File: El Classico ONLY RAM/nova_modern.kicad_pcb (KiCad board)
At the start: 2 copper layers, 379 x 139.7 mm, 49 parts, among them J1 PORTA, J2 PORTB, SW1 SW_SPDT, U1 74LS14, U10 62256P, U11 62256P, U12 27C256, U13 7496, U14 7496, U15 7496, U16 7496, U17 74ALS00, U18 74LS241, U19 74LS241, U2 74LS14, U3 74LS14, U4 74LS14, U5 74LS14, U6 74LS148, U7 74LS148, U8 74LS148, U9 27C256

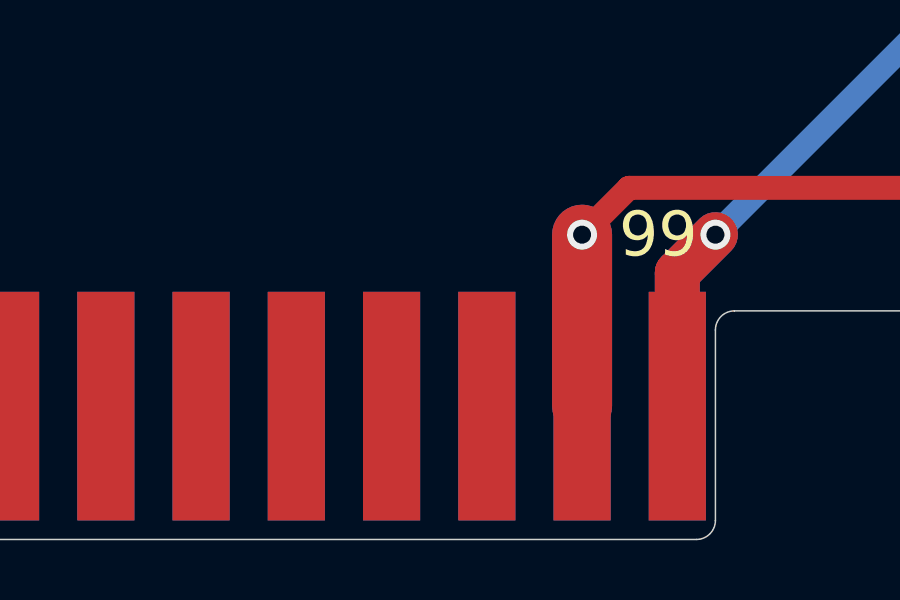
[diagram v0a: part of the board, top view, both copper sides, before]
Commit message: bridge dchp/intp in/out
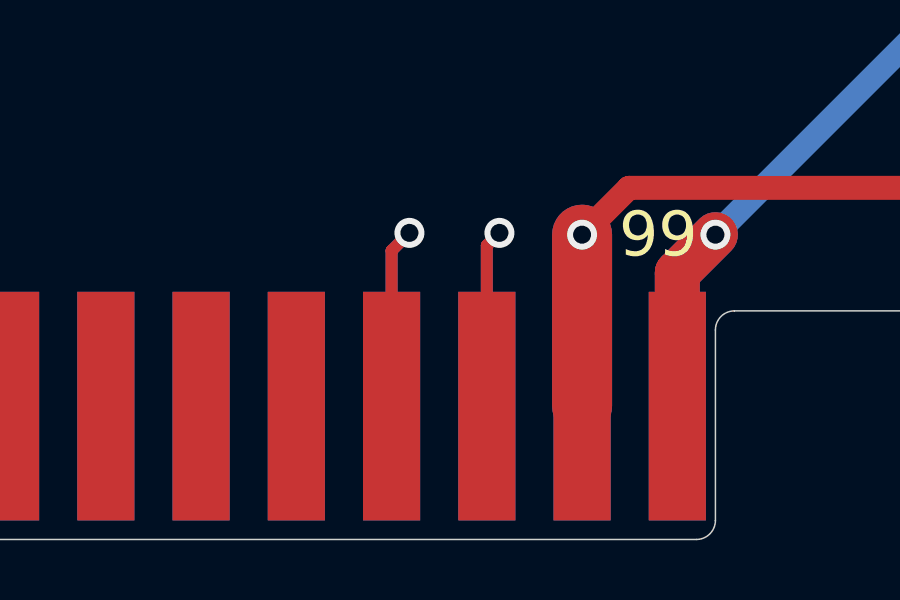
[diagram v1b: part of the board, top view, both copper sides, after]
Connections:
- J1 pad 93: unconnected-(J1-Pin_93-Pad93) -> /dchp
- J1 pad 94: unconnected-(J1-Pin_94-Pad94) -> /dchp
- J1 pad 95: unconnected-(J1-Pin_95-Pad95) -> /intp
- J1 pad 96: unconnected-(J1-Pin_96-Pad96) -> /intp
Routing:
- net /dchp: track 0.00 -> 12.0 mm, vias 0 -> 1
- net /intp: track 0.00 -> 11.9 mm, vias 0 -> 1
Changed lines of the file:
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@@
 			(size 1.905 7.62)
 			(layers "F.Cu" "F.Mask" "F.Paste")
-			(net "unconnected-(J1-Pin_93-Pad93)")
+			(net "/dchp")
 			(pinfunction "Pin_93_93")
-			(pintype "passive+no_connect")
+			(pintype "passive")
 		)
 		(pad "94" smd rect
@@
 			(size 1.905 7.62)
 			(layers "B.Cu" "B.Mask" "B.Paste")
-			(net "unconnected-(J1-Pin_94-Pad94)")
+			(net "/dchp")
 			(pinfunction "Pin_94_94")
-			(pintype "passive+no_connect")
+			(pintype "passive")
 		)
 		(pad "95" smd rect
@@
 			(size 1.905 7.62)
 			(layers "F.Cu" "F.Mask" "F.Paste")
-			(net "unconnected-(J1-Pin_95-Pad95)")
+			(net "/intp")
 			(pinfunction "Pin_95_95")
-			(pintype "passive+no_connect")
+			(pintype "passive")
 		)
 		(pad "96" smd rect
@@
 			(size 1.905 7.62)
 			(layers "B.Cu" "B.Mask" "B.Paste")
-			(net "unconnected-(J1-Pin_96-Pad96)")
+			(net "/intp")
 			(pinfunction "Pin_96_96")
-			(pintype "passive+no_connect")
+			(pintype "passive")
 		)
 		(pad "97" smd rect
@@
 		(net "/WD12")
 	)
+	(segment
+		(start 193 99)
+		(end 192.405 99.595)
+		(width 0.4)
+		(layer "F.Cu")
+		(net "/dchp")
+	)
+	(segment
+		(start 192.405 99.595)
+		(end 192.405 104.775)
+		(width 0.4)
+		(layer "F.Cu")
+		(net "/dchp")
+	)
+	(via
+		(at 193 99)
+		(size 1)
+		(drill 0.6)
+		(layers "F.Cu" "B.Cu")
+		(net "/dchp")
+	)
+	(segment
+		(start 192.405 104.775)
+		(end 192.405 99.595)
+		(width 0.4)
+		(layer "B.Cu")
+		(net "/dchp")
+	)
+	(segment
+		(start 192.405 99.595)
+		(end 193 99)
+		(width 0.4)
+		(layer "B.Cu")
+		(net "/dchp")
+	)
+	(segment
+		(start 195.58 99.42)
+		(end 195.58 104.775)
+		(width 0.4)
+		(layer "F.Cu")
+		(net "/intp")
+	)
+	(segment
+		(start 196 99)
+		(end 195.58 99.42)
+		(width 0.4)
+		(layer "F.Cu")
+		(net "/intp")
+	)
+	(via
+		(at 196 99)
+		(size 1)
+		(drill 0.6)
+		(layers "F.Cu" "B.Cu")
+		(net "/intp")
+	)
+	(segment
+		(start 195.58 99.42)
+		(end 195.58 104.775)
+		(width 0.4)
+		(layer "B.Cu")
+		(net "/intp")
+	)
+	(segment
+		(start 195.58 99.42)
+		(end 196 99)
+		(width 0.4)
+		(layer "B.Cu")
+		(net "/intp")
+	)
 	(zone

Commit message: fix ram card B key + specific parts
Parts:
- J2: footprint _library:portB_NovaMod -> _local:portB_NovaMod
- U17: value 74ALS00 -> 74ALS38
- U18, U19: value 74LS241 -> 74LS244
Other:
- outline, holes or cut-outs redrawn
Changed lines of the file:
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@@
 			(plot_on_all_layers_selection 0x00000000_00000000_00000000_00000000)
 			(disableapertmacros no)
-			(usegerberextensions no)
+			(usegerberextensions yes)
 			(usegerberattributes no)
 			(usegerberadvancedattributes no)
@@
 			(drillshape 0)
 			(scaleselection 1)
-			(outputdirectory "_gerber")
+			(outputdirectory "Gerbers")
 		)
 	)
@@
 		(embedded_fonts no)
 	)
-	(footprint "_library:portB_NovaMod"
+	(footprint "_local:portB_NovaMod"
 		(layer "F.Cu")
 		(at 236.22 104.775)
 		(property "Reference" "J2"
-			(at 158.75 -4.445 0)
+			(at 0 -4.445 0)
 			(layer "F.SilkS")
 			(effects
@@
 		)
 		(pad "51" smd rect
-			(at 79.375 0)
-			(size 1.905 7.62)
+			(at 78.96125 0)
+			(size 1.0775 7.62)
 			(layers "F.Cu" "F.Mask" "F.Paste")
 			(net "unconnected-(J2-Pin_51-Pad51)")
@@
 		)
 		(pad "52" smd rect
-			(at 79.375 0)
-			(size 1.905 7.62)
+			(at 78.96125 0)
+			(size 1.0775 7.62)
 			(layers "B.Cu" "B.Mask" "B.Paste")
 			(net "unconnected-(J2-Pin_52-Pad52)")
@@
 		)
 		(pad "53" smd rect
-			(at 82.55 0)
-			(size 1.905 7.62)
+			(at 83.00125 0)
+			(size 1.0025 7.62)
 			(layers "F.Cu" "F.Mask" "F.Paste")
 			(net "unconnected-(J2-Pin_53-Pad53)")
@@
 		)
 		(pad "54" smd rect
-			(at 82.55 0)
-			(size 1.905 7.62)
+			(at 83.001249 0.000001)
+			(size 1.002498 7.619998)
 			(layers "B.Cu" "B.Mask" "B.Paste")
 			(net "unconnected-(J2-Pin_54-Pad54)")
@@
 		(tags "C Disc series Radial pin pitch 5.00mm  diameter 4.7mm width 2.5mm Capacitor")
 		(property "Reference" "C19"
-			(at 2.5 -2.5 0)
+			(at 2.5 2.64 0)
 			(layer "F.SilkS")
 			(effects
@@
 		(property "Value" "74LS14"
 			(at 3.81 17.57 0)
-			(layer "F.Fab")
+			(layer "F.SilkS")
 			(effects
 				(font
@@
 		(property "Value" "74LS14"
 			(at 3.81 17.57 0)
-			(layer "F.Fab")
+			(layer "F.SilkS")
 			(effects
 				(font
@@
 		(property "Value" "74LS14"
 			(at 3.81 17.57 0)
-			(layer "F.Fab")
+			(layer "F.SilkS")
 			(effects
 				(font
@@
 		(property "Value" "74LS14"
 			(at 3.81 17.57 0)
-			(layer "F.Fab")
+			(layer "F.SilkS")
 			(effects
 				(font
@@
 		(property "Value" "74LS14"
 			(at 3.81 17.57 0)
-			(layer "F.Fab")
+			(layer "F.SilkS")
 			(effects
 				(font
@@
 		(property "Value" "74LS148"
 			(at 3.81 20.11 0)
-			(layer "F.Fab")
+			(layer "F.SilkS")
 			(effects
 				(font
@@
 		(property "Value" "74LS148"
 			(at 3.81 20.11 0)
-			(layer "F.Fab")
+			(layer "F.SilkS")
 			(effects
 				(font
@@
 		(property "Value" "74LS148"
 			(at 3.81 20.11 0)
-			(layer "F.Fab")
+			(layer "F.SilkS")
 			(effects
 				(font
@@
 		(property "Value" "27C256"
 			(at 7.62 35.35 0)
-			(layer "F.Fab")
+			(layer "F.SilkS")
 			(effects
 				(font
@@
 		(property "Value" "62256P"
 			(at 7.62 35.35 0)
-			(layer "F.Fab")
+			(layer "F.SilkS")
 			(effects
 				(font
@@
 		(property "Value" "62256P"
 			(at 7.62 35.35 0)
-			(layer "F.Fab")
+			(layer "F.SilkS")
 			(effects
 				(font
@@
 		(property "Value" "27C256"
 			(at 7.62 35.35 0)
-			(layer "F.Fab")
+			(layer "F.SilkS")
 			(effects
 				(font
@@
 		(property "Value" "7496"
 			(at 3.81 20.11 0)
-			(layer "F.Fab")
+			(layer "F.SilkS")
 			(effects
 				(font
@@
 		(property "Value" "7496"
 			(at 3.81 20.11 0)
-			(layer "F.Fab")
+			(layer "F.SilkS")
 			(effects
 				(font
@@
 		(property "Value" "7496"
 			(at 3.81 20.11 0)
-			(layer "F.Fab")
+			(layer "F.SilkS")
 			(effects
 				(font
@@
 		(property "Value" "7496"
 			(at 3.81 20.11 0)
-			(layer "F.Fab")
+			(layer "F.SilkS")
 			(effects
 				(font
@@
 			)
 		)
-		(property "Value" "74ALS00"
+		(property "Value" "74ALS38"
 			(at 3.81 17.57 0)
-			(layer "F.Fab")
+			(layer "F.SilkS")
 			(effects
 				(font
@@
 			)
 		)
-		(property "Value" "74LS241"
+		(property "Value" "74LS244"
 			(at 3.81 25.19 0)
-			(layer "F.Fab")
+			(layer "F.SilkS")
 			(effects
 				(font
@@
 			)
 		)
-		(property "Value" "74LS241"
+		(property "Value" "74LS244"
 			(at 3.81 25.19 0)
-			(layer "F.Fab")
+			(layer "F.SilkS")
 			(effects
 				(font
@@
 	(gr_line
 		(start 293.37 109.22)
-		(end 392.43 109.22)
+		(end 315.65122 109.234593)
+		(stroke
+			(width 0.05)
+			(type default)
+		)
+		(layer "Edge.Cuts")
+	)
+	(gr_arc
+		(start 316.28622 100.344593)
+		(mid 316.472207 99.89558)
+		(end 316.92122 99.709593)
+		(stroke
+			(width 0.05)
+			(type solid)
+		)
+		(layer "Edge.Cuts")
+	)
+	(gr_arc
+		(start 316.28622 108.599593)
+		(mid 316.100233 109.048606)
+		(end 315.65122 109.234593)
+		(stroke
+			(width 0.05)
+			(type solid)
+		)
+		(layer "Edge.Cuts")
+	)
+	(gr_line
+		(start 316.28622 108.599593)
+		(end 316.28622 100.344593)
+		(stroke
+			(width 0.05)
+			(type solid)
+		)
+		(layer "Edge.Cuts")
+	)
+	(gr_line
+		(start 316.92122 99.709593)
+		(end 317.55622 99.709593)
 		(stroke
 			(width 0.05)
@@
 	)
 	(gr_arc
+		(start 317.55622 99.709593)
+		(mid 318.005233 99.89558)
+		(end 318.19122 100.344593)
+		(stroke
+			(width 0.05)
+			(type solid)
+		)
+		(layer "Edge.Cuts")
+	)
+	(gr_line
+		(start 318.19122 100.344593)
+		(end 318.19122 108.599593)
+		(stroke
+			(width 0.05)
+			(type solid)
+		)
+		(layer "Edge.Cuts")
+	)
+	(gr_arc
+		(start 318.82622 109.234593)
+		(mid 318.377207 109.048606)
+		(end 318.19122 108.599593)
+		(stroke
+			(width 0.05)
+			(type solid)
+		)
+		(layer "Edge.Cuts")
+	)
+	(gr_line
+		(start 318.82622 109.234593)
+		(end 392.43 109.22)
+		(stroke
+			(width 0.05)
+			(type default)
+		)
+		(layer "Edge.Cuts")
+	)
+	(gr_arc
 		(start 393.065 102.235)
 		(mid 393.250987 101.785987)
@@
 	)
 	(segment
+		(start 193 99)
+		(end 192.405 99.595)
+		(width 0.4)
+		(layer "F.Cu")
+		(net "/dchp")
+	)
+	(segment
+		(start 192.405 99.595)
+		(end 192.405 104.775)
+		(width 0.4)
+		(layer "F.Cu")
+		(net "/dchp")
+	)
+	(via
+		(at 193 99)
+		(size 1)
+		(drill 0.6)
+		(layers "F.Cu" "B.Cu")
+		(net "/dchp")
+	)
+	(segment
+		(start 192.405 104.775)
+		(end 192.405 99.595)
+		(width 0.4)
+		(layer "B.Cu")
+		(net "/dchp")
+	)
+	(segment
+		(start 192.405 99.595)
+		(end 193 99)
+		(width 0.4)
+		(layer "B.Cu")
+		(net "/dchp")
+	)
+	(segment
+		(start 195.58 99.42)
+		(end 195.58 104.775)
+		(width 0.4)
+		(layer "F.Cu")
+		(net "/intp")
+	)
+	(segment
+		(start 196 99)
+		(end 195.58 99.42)
+		(width 0.4)
+		(layer "F.Cu")
+		(net "/intp")
+	)
+	(via
+		(at 196 99)
+		(size 1)
+		(drill 0.6)
+		(layers "F.Cu" "B.Cu")
+		(net "/intp")
+	)
+	(segment
+		(start 195.58 99.42)
+		(end 195.58 104.775)
+		(width 0.4)
+		(layer "B.Cu")
+		(net "/intp")
+	)
+	(segment
+		(start 195.58 99.42)
+		(end 196 99)
+		(width 0.4)
+		(layer "B.Cu")
+		(net "/intp")
+	)
+	(segment
 		(start 344.17 -14.605)
 		(end 305.71765 -14.605)
@@
 		(net "/WD12")
 	)
-	(segment
-		(start 193 99)
-		(end 192.405 99.595)
-		(width 0.4)
-		(layer "F.Cu")
-		(net "/dchp")
-	)
-	(segment
-		(start 192.405 99.595)
-		(end 192.405 104.775)
-		(width 0.4)
-		(layer "F.Cu")
-		(net "/dchp")
-	)
-	(via
-		(at 193 99)
-		(size 1)
-		(drill 0.6)
-		(layers "F.Cu" "B.Cu")
-		(net "/dchp")
-	)
-	(segment
-		(start 192.405 104.775)
-		(end 192.405 99.595)
-		(width 0.4)
-		(layer "B.Cu")
-		(net "/dchp")
-	)
-	(segment
-		(start 192.405 99.595)
-		(end 193 99)
-		(width 0.4)
-		(layer "B.Cu")
-		(net "/dchp")
-	)
-	(segment
-		(start 195.58 99.42)
-		(end 195.58 104.775)
-		(width 0.4)
-		(layer "F.Cu")
-		(net "/intp")
-	)
-	(segment
-		(start 196 99)
-		(end 195.58 99.42)
-		(width 0.4)
-		(layer "F.Cu")
-		(net "/intp")
-	)
-	(via
-		(at 196 99)
-		(size 1)
-		(drill 0.6)
-		(layers "F.Cu" "B.Cu")
-		(net "/intp")
-	)
-	(segment
-		(start 195.58 99.42)
-		(end 195.58 104.775)
-		(width 0.4)
-		(layer "B.Cu")
-		(net "/intp")
-	)
-	(segment
-		(start 195.58 99.42)
-		(end 196 99)
-		(width 0.4)
-		(layer "B.Cu")
-		(net "/intp")
-	)
 	(zone
